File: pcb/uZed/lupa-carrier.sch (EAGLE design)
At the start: 20 parts

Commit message: more work on carrier test
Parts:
- added C10, C8, C9: .1uF, rcl:C-USC0603
- added JP1: (no value), pinhead:PINHD-1X2
- added K1: 694108105102, Wurth_Elektronik_Electromechanic_DC_Power_Jack_Connectors_rev15c:694108105102
- added R10: 120, rcl:R-US_R0603
- added R11, R13, R14, R8: 1k, rcl:R-US_R0603
- added R12: 1k5, rcl:R-US_R0603
- added R15: 3k74, rcl:R-US_R0603
- added R16: 0, rcl:R-US_R0603
- added R17: 3k, rcl:R-US_R0603
- added R18: 100k, rcl:R-US_R0603
- added R5: 45k3, rcl:R-US_R0603
- added R6: 10k, rcl:R-US_R0603
- added R7: 3k92, rcl:R-US_R0603
- added R9: 220, rcl:R-US_R0603
- added U$10: AP331A, lupa300-components:AP331A
- added U$8: BAT54L, lupa300-components:BAT54L
- added U$9: TL431A, lupa300-components:TL431A
- U$7: value BERGSTAK-100POS -> BSS138; device lupa300-components:BERGSTAK-100POS -> lupa300-components:BSS138
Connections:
- net PGOOD_CARRIER renamed PG_CARRIER
- removed net 3V3: JX1.P$78, JX1.P$80, JX2.P$78, JX2.P$80
- removed net HDMI_CLOCK: JX1.P$41
- new net 2V5_REF: C8.1, R11.2, R12.1, U$9.K, U$9.REF
- new net N$8: R9.1, U$8.A
- new net N$9: C10.2, R16.1, R17.1, U$10.VOUT
- net 5V: now also JX2.P$12, R17.2, R8.2, R9.2
- net 5V_OFF: now also R7.2, U$7.G
- net GND: now also C8.2, C9.2, JX1.P$77, JX2.P$77, K1.2, K1.3, R10.2, R13.1, R15.2, R18.1, R6.1, R7.1, U$10.VSS, U$7.S, U$9.A
- net N$2: now also R5.1, R6.2, U$4.FB; no longer U$7.P$5
- net N$5: now also R12.2, R13.2, U$10.P; no longer U$7.P$16, U$7.P$22, U$7.P$28, U$7.P$34, U$7.P$40, U$7.P$46, U$7.P$52, U$7.P$66
- net N$6: now also JP1.1, R8.1; no longer U$7.P$15
- net N$7: now also C10.1, R14.2, R15.1, U$10.N; no longer U$7.P$58, U$7.P$60
- net VADJ_EN: now also R16.2, R18.2
- net VCCIO: now also JX1.P$78, JX1.P$79, JX1.P$80, JX2.P$78, JX2.P$79, JX2.P$80, R5.2
- net VCCIO_EN: now also JP1.2, R10.1, R14.1, U$7.D, U$8.C
- net VIN: now also C9.1, K1.1, R11.1, U$10.VDD
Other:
- moved on the sheet: JX1, JX2

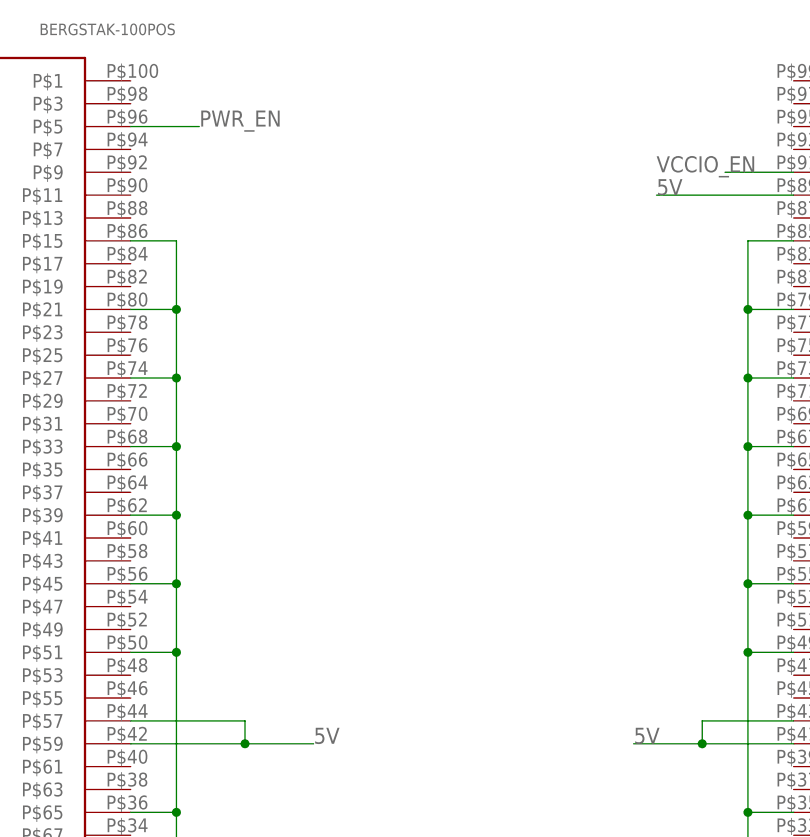
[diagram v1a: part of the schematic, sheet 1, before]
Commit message: tweaked layout, ready to fab
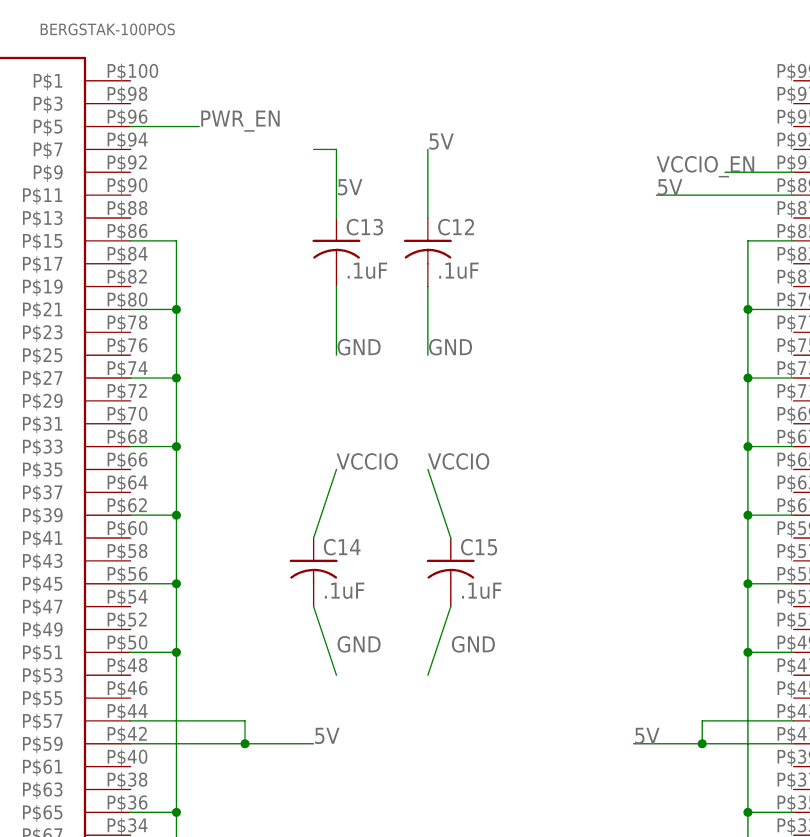
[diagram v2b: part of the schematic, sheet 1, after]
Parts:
- added C12, C13, C14, C15: .1uF, rcl:C-USC0603
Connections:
- net 5V: now also C12.1, C13.1
- net GND: now also C12.2, C13.2, C14.2, C15.2
- net VCCIO: now also C14.1, C15.1
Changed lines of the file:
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@@
 <?xml version="1.0" encoding="utf-8"?>
 <!DOCTYPE eagle SYSTEM "eagle.dtd">
-<eagle version="8.6.1">
+<eagle version="8.7.0">
 <drawing>
 <settings>
@@
 <part name="K1" library="Wurth_Elektronik_Electromechanic_DC_Power_Jack_Connectors_rev15c" deviceset="694108105102" device=""/>
 <part name="SUPPLY26" library="supply2" library_urn="urn:adsk.eagle:library:372" deviceset="GND" device=""/>
+<part name="C12" library="rcl" library_urn="urn:adsk.eagle:library:334" deviceset="C-US" device="C0603" package3d_urn="urn:adsk.eagle:package:23616/2" value=".1uF"/>
+<part name="C13" library="rcl" library_urn="urn:adsk.eagle:library:334" deviceset="C-US" device="C0603" package3d_urn="urn:adsk.eagle:package:23616/2" value=".1uF"/>
+<part name="C14" library="rcl" library_urn="urn:adsk.eagle:library:334" deviceset="C-US" device="C0603" package3d_urn="urn:adsk.eagle:package:23616/2" value=".1uF"/>
+<part name="C15" library="rcl" library_urn="urn:adsk.eagle:library:334" deviceset="C-US" device="C0603" package3d_urn="urn:adsk.eagle:package:23616/2" value=".1uF"/>
 </parts>
 <sheets>
@@
 <instance part="SUPPLY14" gate="GND" x="124.46" y="12.7"/>
 <instance part="SUPPLY15" gate="GND" x="162.56" y="12.7"/>
+<instance part="C12" gate="G$1" x="88.9" y="134.62"/>
+<instance part="C13" gate="G$1" x="78.74" y="134.62"/>
+<instance part="C14" gate="G$1" x="76.2" y="99.06"/>
+<instance part="C15" gate="G$1" x="91.44" y="99.06"/>
 </instances>
 <busses>
@@
 <junction x="162.56" y="38.1"/>
 </segment>
+<segment>
+<pinref part="C12" gate="G$1" pin="2"/>
+<wire x1="88.9" y1="129.54" x2="88.9" y2="121.92" width="0.1524" layer="91"/>
+<label x="88.9" y="121.92" size="1.778" layer="95"/>
+</segment>
+<segment>
+<pinref part="C13" gate="G$1" pin="2"/>
+<wire x1="78.74" y1="129.54" x2="78.74" y2="121.92" width="0.1524" layer="91"/>
+<label x="78.74" y="121.92" size="1.778" layer="95"/>
+</segment>
+<segment>
+<pinref part="C15" gate="G$1" pin="2"/>
+<wire x1="91.44" y1="93.98" x2="88.9" y2="86.36" width="0.1524" layer="91"/>
+<label x="91.44" y="88.9" size="1.778" layer="95"/>
+</segment>
+<segment>
+<pinref part="C14" gate="G$1" pin="2"/>
+<wire x1="76.2" y1="93.98" x2="78.74" y2="86.36" width="0.1524" layer="91"/>
+<label x="78.74" y="88.9" size="1.778" layer="95"/>
+</segment>
 </net>
 <net name="PWR_EN" class="0">
@@
 <label x="114.3" y="139.7" size="1.778" layer="95"/>
 </segment>
+<segment>
+<pinref part="C12" gate="G$1" pin="1"/>
+<wire x1="88.9" y1="137.16" x2="88.9" y2="144.78" width="0.1524" layer="91"/>
+<label x="88.9" y="144.78" size="1.778" layer="95"/>
+</segment>
+<segment>
+<pinref part="C13" gate="G$1" pin="1"/>
+<wire x1="78.74" y1="137.16" x2="78.74" y2="144.78" width="0.1524" layer="91"/>
+<wire x1="78.74" y1="144.78" x2="76.2" y2="144.78" width="0.1524" layer="91"/>
+<label x="78.74" y="139.7" size="1.778" layer="95"/>
+</segment>
 </net>
 <net name="VCCIO_EN" class="0">
@@
 <label x="177.8" y="53.34" size="1.778" layer="95"/>
 </segment>
+<segment>
+<pinref part="C14" gate="G$1" pin="1"/>
+<wire x1="76.2" y1="101.6" x2="78.74" y2="109.22" width="0.1524" layer="91"/>
+<label x="78.74" y="109.22" size="1.778" layer="95"/>
+</segment>
+<segment>
+<pinref part="C15" gate="G$1" pin="1"/>
+<wire x1="91.44" y1="101.6" x2="88.9" y2="109.22" width="0.1524" layer="91"/>
+<label x="88.9" y="109.22" size="1.778" layer="95"/>
+</segment>
 </net>

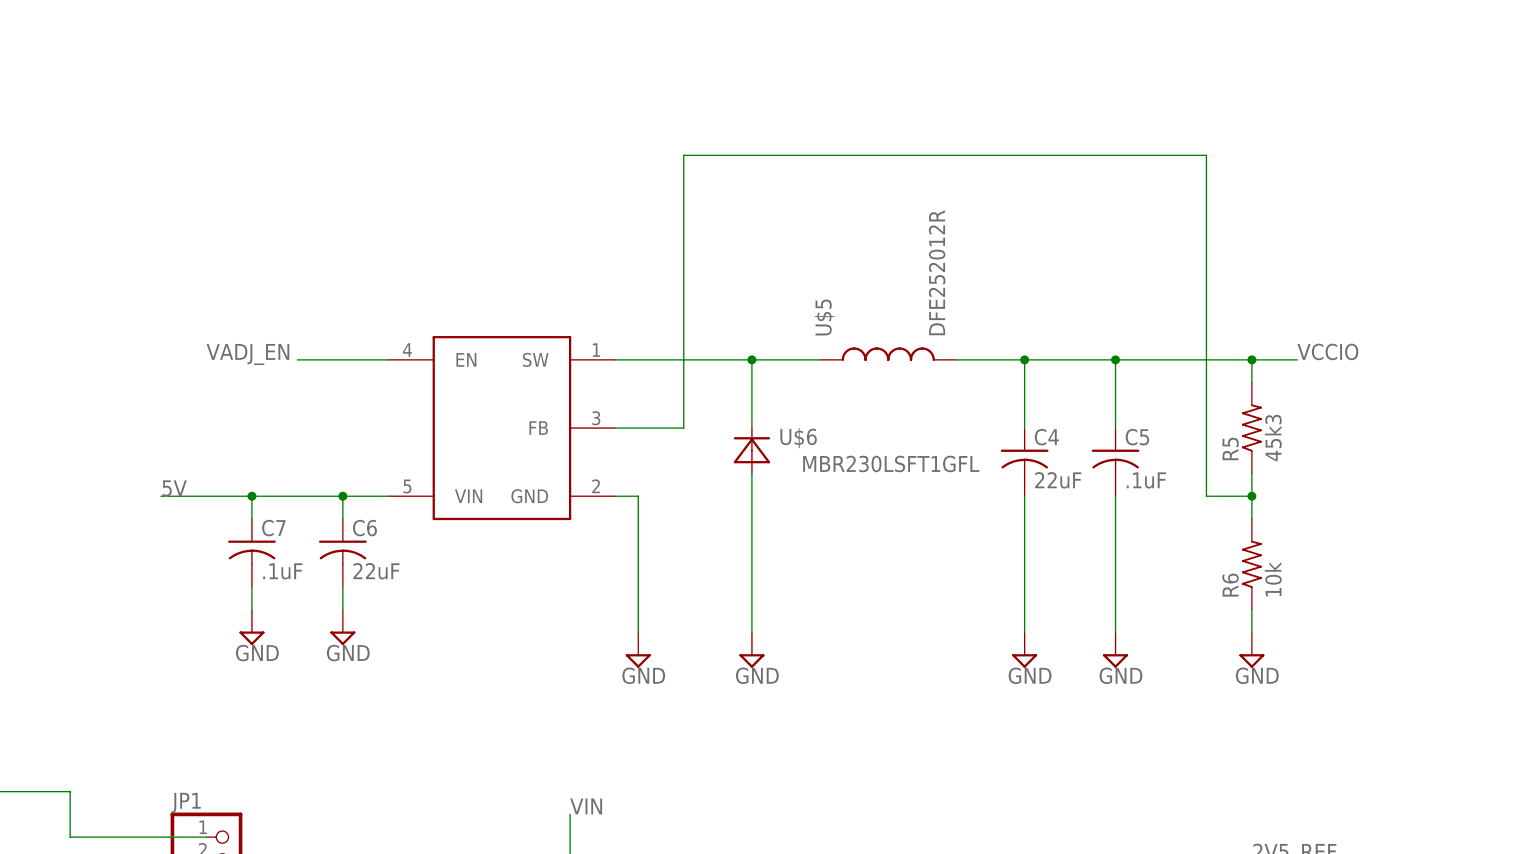
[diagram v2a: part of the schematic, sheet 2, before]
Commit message: added 2A 3.3v reg to power suply design. made power supply layout more compact. increased board size
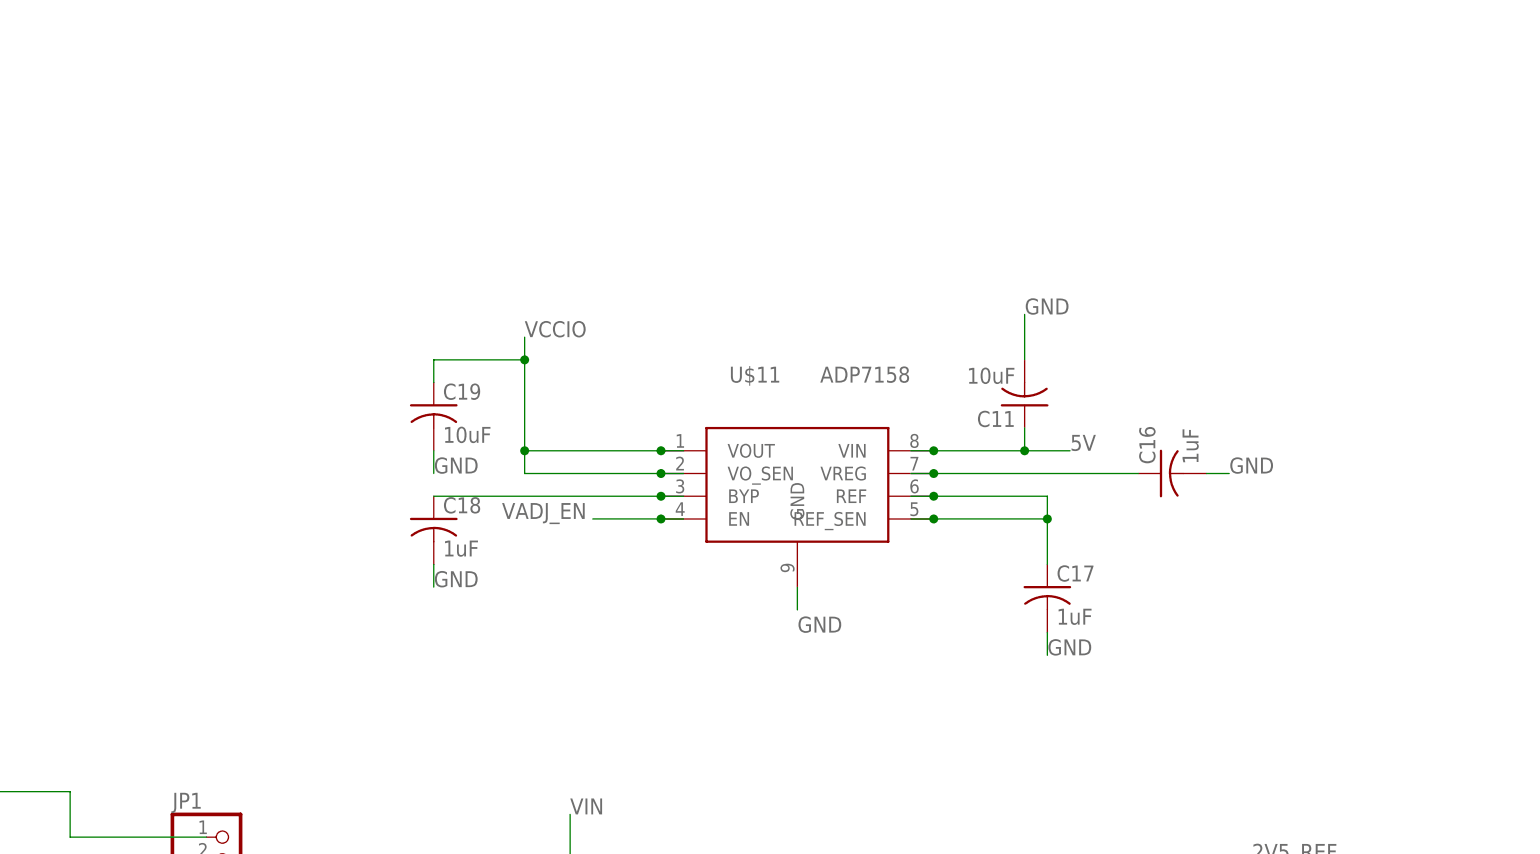
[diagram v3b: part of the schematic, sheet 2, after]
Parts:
- removed C4, C6: 22uF, rcl:C-USC1206
- removed C5, C7: .1uF, rcl:C-USC0603
- removed R5: 45k3, rcl:R-US_R0603
- removed R6: 10k, rcl:R-US_R0603
- removed U$4: LMR10510, lupa300-components:LMR10510
- removed U$5: DFE252012R, lupa300-components:DFE252012R
- removed U$6: MBR230LSFT1GFL, lupa300-components:MBR230LSFT1GFL
- added C11, C19: 10uF, rcl:C-USC0603
- added C16, C17, C18: 1uF, rcl:C-USC0603
- added U$11: ADP7158, lupa300-components:ADP7158
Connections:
- removed net N$2: R5.1, R6.2, U$4.FB
- removed net N$3: U$4.SW, U$5.1, U$6.C
- new net N$10: C16.1, U$11.VREG
- new net N$11: C17.1, U$11.REF, U$11.REF_SEN
- new net N$12: C18.1, U$11.BYP
- net 5V: now also C11.1, U$11.VIN; no longer C6.1, C7.1, U$4.VIN
- net GND: now also C11.2, C16.2, C17.2, C18.2, C19.2, U$11.GND; no longer C4.2, C5.2, C6.2, C7.2, R6.1, U$4.GND, U$6.A
- net VADJ_EN: now also U$11.EN; no longer U$4.EN
- net VCCIO: now also C19.1, U$11.VOUT, U$11.VO_SEN; no longer C4.1, C5.1, R5.2, U$5.2

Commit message: more lupa crrier layout work
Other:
- moved on the sheet: C12, C13, C14, C15, JX1, JX2

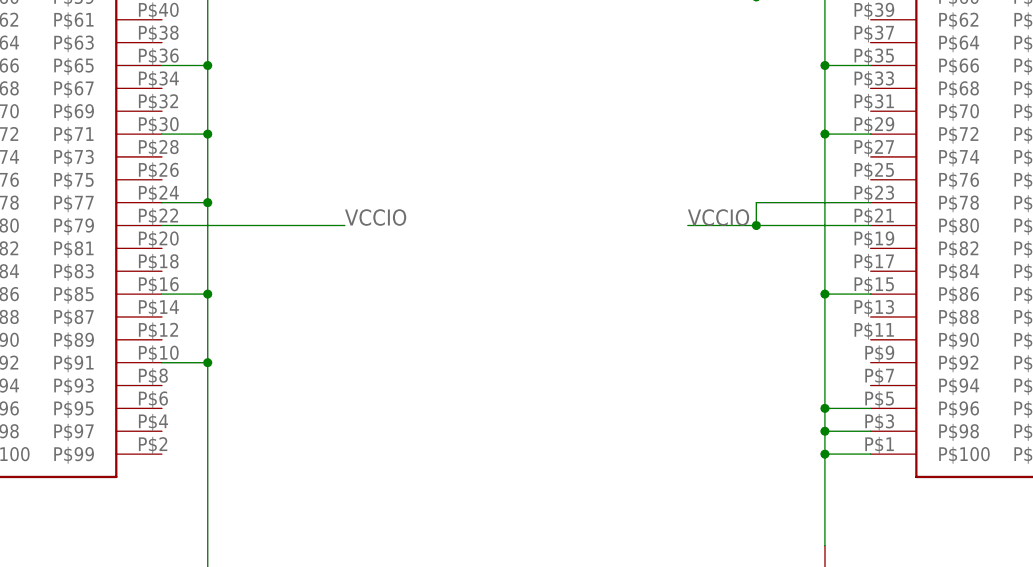
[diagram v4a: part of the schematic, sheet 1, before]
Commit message: ordered 5 from pcbway as is
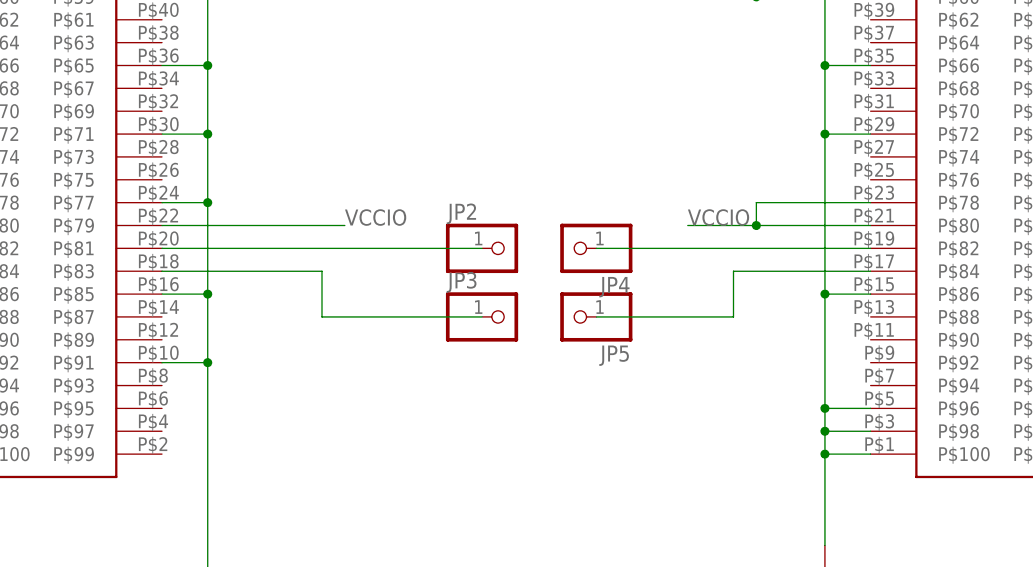
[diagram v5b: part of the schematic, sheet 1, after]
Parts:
- added JP2, JP3, JP4, JP5: (no value), pinhead:PINHD-1X1
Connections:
- new net N$13: JP2.1, JX2.P$81
- new net N$14: JP3.1, JX2.P$83
- new net N$15: JP4.1, JX1.P$82
- new net N$16: JP5.1, JX1.P$84
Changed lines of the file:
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@@
 <part name="C18" library="rcl" library_urn="urn:adsk.eagle:library:334" deviceset="C-US" device="C0603" package3d_urn="urn:adsk.eagle:package:23616/2" value="1uF"/>
 <part name="C19" library="rcl" library_urn="urn:adsk.eagle:library:334" deviceset="C-US" device="C0603" package3d_urn="urn:adsk.eagle:package:23616/2" value="10uF"/>
+<part name="JP2" library="pinhead" library_urn="urn:adsk.eagle:library:325" deviceset="PINHD-1X1" device="" package3d_urn="urn:adsk.eagle:package:22485/2"/>
+<part name="JP3" library="pinhead" library_urn="urn:adsk.eagle:library:325" deviceset="PINHD-1X1" device="" package3d_urn="urn:adsk.eagle:package:22485/2"/>
+<part name="JP4" library="pinhead" library_urn="urn:adsk.eagle:library:325" deviceset="PINHD-1X1" device="" package3d_urn="urn:adsk.eagle:package:22485/2"/>
+<part name="JP5" library="pinhead" library_urn="urn:adsk.eagle:library:325" deviceset="PINHD-1X1" device="" package3d_urn="urn:adsk.eagle:package:22485/2"/>
 </parts>
 <sheets>
@@
 <instance part="C14" gate="G$1" x="99.06" y="180.34"/>
 <instance part="C15" gate="G$1" x="114.3" y="180.34"/>
+<instance part="JP2" gate="G$1" x="101.6" y="48.26"/>
+<instance part="JP3" gate="G$1" x="101.6" y="40.64"/>
+<instance part="JP4" gate="G$1" x="109.22" y="48.26" rot="R180"/>
+<instance part="JP5" gate="G$1" x="109.22" y="40.64" rot="R180"/>
 </instances>
 <busses>
@@
 </segment>
 </net>
+<net name="N$13" class="0">
+<segment>
+<pinref part="JP2" gate="G$1" pin="1"/>
+<pinref part="JX2" gate="G$1" pin="P$81"/>
+<wire x1="99.06" y1="48.26" x2="63.5" y2="48.26" width="0.1524" layer="91"/>
+</segment>
+</net>
+<net name="N$14" class="0">
+<segment>
+<pinref part="JP3" gate="G$1" pin="1"/>
+<wire x1="99.06" y1="40.64" x2="81.28" y2="40.64" width="0.1524" layer="91"/>
+<wire x1="81.28" y1="40.64" x2="81.28" y2="45.72" width="0.1524" layer="91"/>
+<pinref part="JX2" gate="G$1" pin="P$83"/>
+<wire x1="81.28" y1="45.72" x2="63.5" y2="45.72" width="0.1524" layer="91"/>
+</segment>
+</net>
+<net name="N$15" class="0">
+<segment>
+<pinref part="JP4" gate="G$1" pin="1"/>
+<pinref part="JX1" gate="G$1" pin="P$82"/>
+<wire x1="111.76" y1="48.26" x2="142.24" y2="48.26" width="0.1524" layer="91"/>
+</segment>
+</net>
+<net name="N$16" class="0">
+<segment>
+<pinref part="JP5" gate="G$1" pin="1"/>
+<wire x1="111.76" y1="40.64" x2="127" y2="40.64" width="0.1524" layer="91"/>
+<wire x1="127" y1="40.64" x2="127" y2="45.72" width="0.1524" layer="91"/>
+<pinref part="JX1" gate="G$1" pin="P$84"/>
+<wire x1="127" y1="45.72" x2="142.24" y2="45.72" width="0.1524" layer="91"/>
+</segment>
+</net>

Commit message: started lupa300 integration, converted to 4 layer
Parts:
- removed JP2, JP3, JP4, JP5: (no value), pinhead:PINHD-1X1
- added C20, C21, C4, C6, C7: 0.1uF, rcl:C-EUC0603
- added C5: .1uF, rcl:C-EUC0603
- added R19: 110k, rcl:R-US_R0603
- added R20: 42k, rcl:R-US_R0603
- added R21: 1.5M, rcl:R-US_R0603
- added R22: 500k, rcl:R-US_R0603
- added R5: 68k, rcl:R-US_R0603
- added R6: 10k, rcl:R-US_R0603
- added U$4: (no value), andon:LUPA300
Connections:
- removed net N$13: JP2.1, JX2.P$81
- removed net N$14: JP3.1, JX2.P$83
- removed net N$15: JP4.1, JX1.P$82
- removed net N$16: JP5.1, JX1.P$84
- new net ADC_BIAS: C4.1, R6.2, U$4.ADC_BIAS
- new net BIAS1: C21.1, R22.2, U$4.BIAS1
- new net BIAS2: C20.1, R21.2, U$4.BIAS2
- new net BIAS3: C6.1, R20.2, U$4.BIAS3
- new net BIAS4: C5.1, R19.2, U$4.BIAS4
- new net CLK: U$4.CLK
- new net D0: U$4.D0
- new net D1: U$4.D1
- new net D2: U$4.D2
- new net D3: U$4.D3
- new net D4: U$4.D4
- new net D5: U$4.D5
- new net D6: U$4.D6
- new net D7: U$4.D7
- new net D8: U$4.D8
- new net D9: U$4.D9
- new net FRAME_VALID: U$4.FRAME_VALID
- new net INT_TIME1: U$4.INT_TIME_1
- new net INT_TIME2: U$4.INT_TIME_2
- new net INT_TIME3: U$4.INT_TIME_3
- new net LINE_VALID: U$4.LINE_VALID
- new net PRECHARGE_BIAS: C7.1, R5.2, U$4.PRECHARGE_BIAS
- new net RESET: U$4.RESET_N
- new net SPI_CLK: U$4.SPI_CLK
- new net SPI_DATA: U$4.SPI_DATA
- new net SPI_EN: U$4.SPI_EN
- new net VADC: R6.1, U$4.VADC, U$4.VADC1, U$4.VADC2
- new net VDDA: R19.1, R20.1, R21.1, R22.1, U$4.VDDA, U$4.VDDA1
- new net VDDD: U$4.VDDD, U$4.VDDD1
- new net VDDO: U$4.VDDO
- new net VMEM_H: U$4.VMEM_H
- new net VPIX: R5.1, U$4.VPIX
- new net VRESET_1: U$4.VRESET_1
- new net VRESET_2: U$4.VRESET_2
- new net VRESET_3: U$4.VRESET_3
- net GND: now also C20.2, C21.2, C4.2, C5.2, C6.2, C7.2, U$4.GNDA, U$4.GNDA1, U$4.GNDA2, U$4.GNDADC, U$4.GNDADC1, U$4.GNDD, U$4.GNDD1, U$4.GNDO, U$4.GND_DRIVERS
